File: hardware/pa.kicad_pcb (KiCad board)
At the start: 2 copper layers, 100 x 80 mm, 91 parts, among them J1 Conn_Coaxial, J11 RXSupply, J2 FromRX, J3 Barrel_Jack_Switch, J6 RX-HF, J7 TX-HF, K1 G6S-2, K2 G6S-2, K3 G6S-2, K4 G6S-2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

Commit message: Added quick-set.
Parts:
- removed C30: 100n, Capacitor_THT:C_Disc_D3.0mm_W2.0mm_P2.50mm
- added C31: 100n, Capacitor_THT:C_Disc_D4.7mm_W2.5mm_P5.00mm, F.Cu at (107.8, 100.7)
- added D6: 1n4148, Diode_THT:D_T-1_P2.54mm_Vertical_AnodeUp, F.Cu at (82.4, 72.8)
- added D7: 1n4148, Diode_THT:D_T-1_P2.54mm_Vertical_AnodeUp, F.Cu at (79.8, 70.3)
- added L14: 22u, Inductor_THT:L_Radial_D8.7mm_P5.00mm_Fastron_07HCP, F.Cu at (107.8, 62.7)
- C12, C17, C4, C7: value 330p -> 470p
- C13, C8: value 680p -> 1n
- C14, C9: value 1n -> 1.5n
- C16, C3: value 150p -> 220p
- C18, C5: value 470p -> 820p
- L1, L9: value 440n -> 330n
- L10, L2: value 650n -> 480n
- L11, L3: value 1330n -> 750n
- L12, L4: value 2050n -> 1700n
- L5: value 520n -> 330n
- L6: value 760n -> 480n
- L7: value 1530n -> 750n
- L8: value 3000n -> 1700n
- Q5: value BD140 -> BD140-16
- Q6: value BS170 -> 4 x BS170
- moved C24 48.5 mm to (102.8, 52.5), turned to 0 degrees
- moved D1 5.09 mm to (112.8, 67.5), turned to 0 degrees
- moved D3 5.08 mm to (150.9, 67.8), turned to 0 degrees
- moved D5 5.08 mm to (138.2, 67.8), turned to 0 degrees
- moved D2 5.08 mm to (125.5, 67.8), turned to 0 degrees
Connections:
- C26 pad 1: VCC -> Net-(C26-Pad1)
- K1 pad 1: RL10M -> +12V
- K1 pad 10: Net-(K1-Pad10) -> GND
- K1 pad 12: +12V -> RL10M
- K1 pad 3: Net-(K1-Pad3) -> GND
- K1 pad 4: LPF -> Net-(C15-Pad1)
- K1 pad 5: Net-(C15-Pad1) -> LPF
- K1 pad 8: Net-(C2-Pad1) -> Net-(J1-Pad1)
- K1 pad 9: Net-(J1-Pad1) -> Net-(C2-Pad1)
- K2 pad 1: RL20M -> +12V
- K2 pad 10: Net-(K2-Pad10) -> GND
- K2 pad 12: +12V -> RL20M
- K2 pad 3: Net-(K2-Pad3) -> GND
- K2 pad 4: LPF -> Net-(C16-Pad1)
- K2 pad 5: Net-(C16-Pad1) -> LPF
- K2 pad 8: Net-(C3-Pad1) -> Net-(J1-Pad1)
- K2 pad 9: Net-(J1-Pad1) -> Net-(C3-Pad1)
- K3 pad 1: RL40M -> +12V
- K3 pad 10: Net-(K3-Pad10) -> GND
- K3 pad 12: +12V -> RL40M
- K3 pad 3: Net-(K3-Pad3) -> GND
- K3 pad 4: LPF -> Net-(C17-Pad1)
- K3 pad 5: Net-(C17-Pad1) -> LPF
- K3 pad 8: Net-(C4-Pad1) -> Net-(J1-Pad1)
- K3 pad 9: Net-(J1-Pad1) -> Net-(C4-Pad1)
- K4 pad 1: RL80M -> +12V
- K4 pad 10: Net-(K4-Pad10) -> GND
- K4 pad 12: +12V -> RL80M
- K4 pad 3: Net-(K4-Pad3) -> GND
- K4 pad 4: LPF -> Net-(C18-Pad1)
- K4 pad 5: Net-(C18-Pad1) -> LPF
- K4 pad 8: Net-(C5-Pad1) -> Net-(J1-Pad1)
- K4 pad 9: Net-(J1-Pad1) -> Net-(C5-Pad1)
- Q5 pad 1: VCC -> Net-(C26-Pad1)
- R9 pad 2: VCC -> Net-(C26-Pad1)
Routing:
- net VCC: track 109.3 -> 68.1 mm, vias 1 -> 0
- net Net-(C26-Pad1): track 0.00 -> 39.2 mm
- net Net-(J1-Pad1): track 72.4 -> 63.1 mm, vias 0 -> 1
- net +12V: track 86.1 -> 78.9 mm
- net LPF: track 77.1 -> 84.1 mm
- net RL10M: track 50.8 -> 56.7 mm
- net RL80M: track 50.8 -> 56.5 mm
- net RL40M: track 50.8 -> 56.5 mm
- net RL20M: track 50.8 -> 56.5 mm
- net Net-(C18-Pad1): track 33.0 -> 36.8 mm
- net Net-(C15-Pad1): track 27.9 -> 31.7 mm
- net Net-(C16-Pad1): track 33.0 -> 36.8 mm
- net Net-(C17-Pad1): track 27.9 -> 31.7 mm
- net Net-(Q8-Pad2): track 7.66 -> 5.08 mm
- net Net-(C5-Pad1): track 8.67 -> 11.2 mm
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
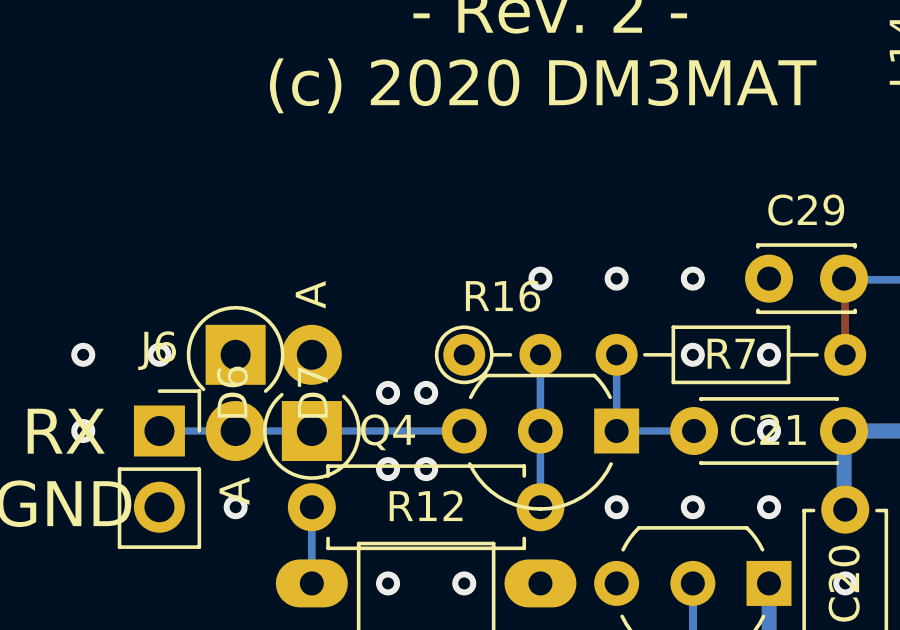
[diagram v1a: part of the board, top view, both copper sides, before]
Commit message: Fixed RX/TX sw. on PA.
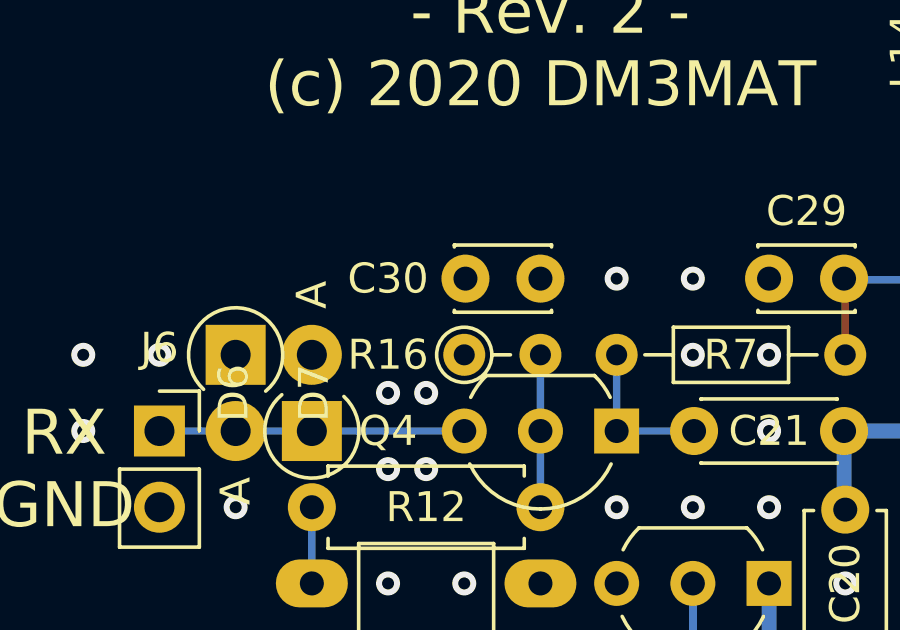
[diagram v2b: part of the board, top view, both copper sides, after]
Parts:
- added C30: 100n, Capacitor_THT:C_Disc_D3.0mm_W2.0mm_P2.50mm, F.Cu at (90.0, 67.8)
- Q6: value 4 x BS170 -> BS170
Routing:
- net GND: vias 226 -> 225

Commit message: Fixed docs.
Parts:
- moved C16 32.5 mm to (157.3, 112.9)
- moved C24 32.5 mm to (134.5, 59.5)
- moved C25 32.5 mm to (129.4, 110.3)
- moved C26 32.5 mm to (139.5, 84.9)
- moved C29 32.5 mm to (129.4, 74.8)
- moved C31 32.5 mm to (139.5, 107.7)
- moved D2 32.5 mm to (157.3, 74.8)
- moved K2 32.5 mm to (157.3, 77.3)
- moved L14 32.5 mm to (139.5, 69.7)
- moved Q11 32.5 mm to (129.4, 84.9)
- moved Q6 32.5 mm to (129.4, 100.2)
- moved Q7 32.5 mm to (129.4, 95.1)
- moved Q9 32.5 mm to (129.4, 90.0)
- moved R1 32.5 mm to (139.5, 128.1)
- moved R4 32.5 mm to (157.3, 125.6)
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
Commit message: Fixed PA.
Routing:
- net Net-(C30-Pad1): track 5.08 -> 7.62 mm
